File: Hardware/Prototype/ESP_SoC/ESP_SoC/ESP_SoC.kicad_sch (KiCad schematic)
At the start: 35 parts, among them J1 USB_A, J2 Conn_01x01, J3 Conn_01x01, P1 USB_C_Plug, SW1 RESET, SW2 BOOT, U1 AP2112K-3.3, U2 ESP32-S3FN8, Y1 40MHz

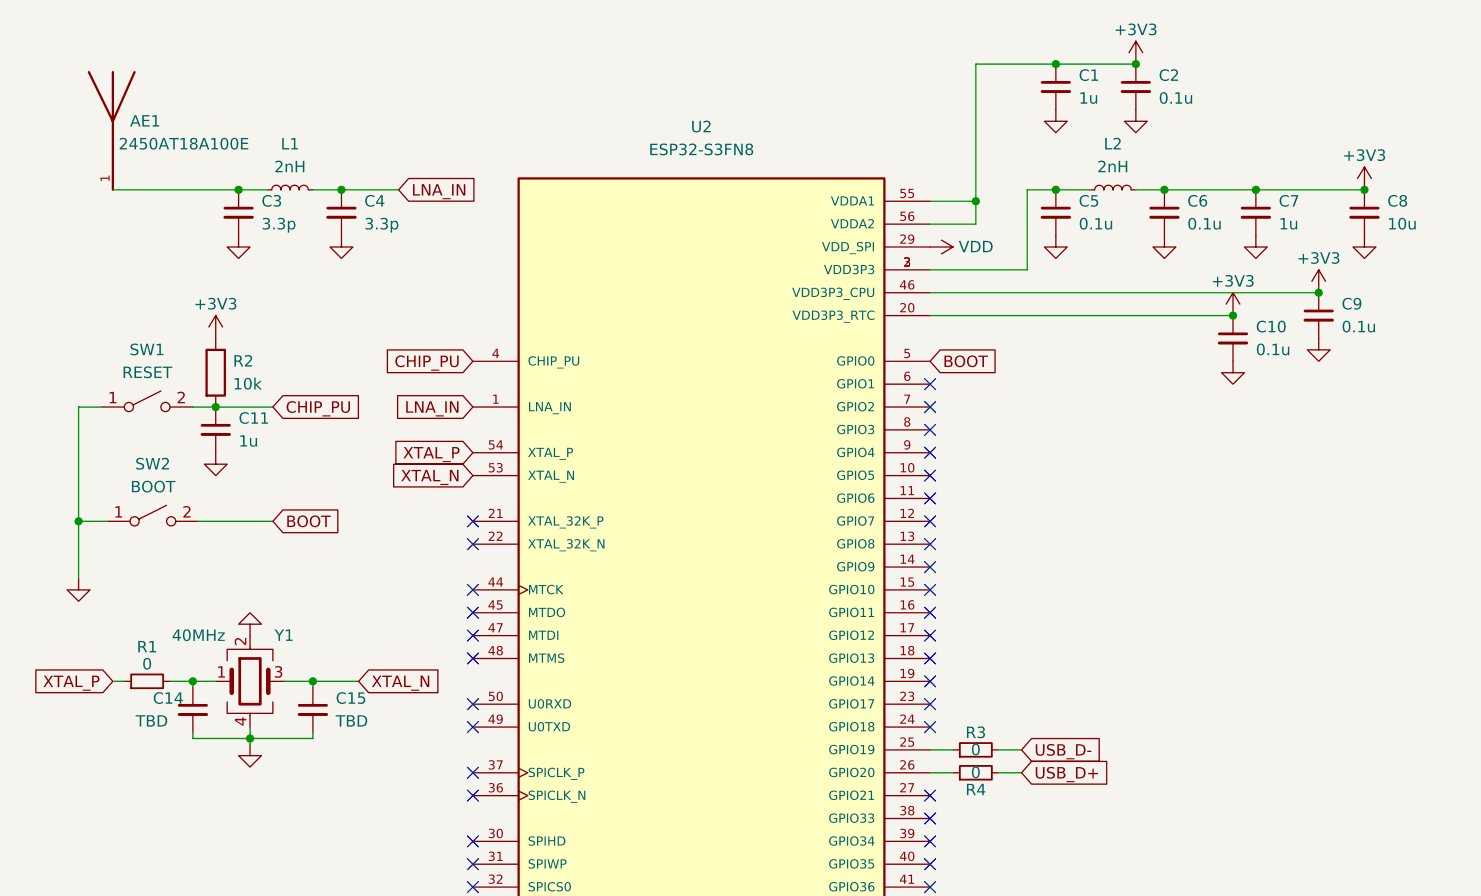
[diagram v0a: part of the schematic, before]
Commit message: Finished PCB prototypes and BOM
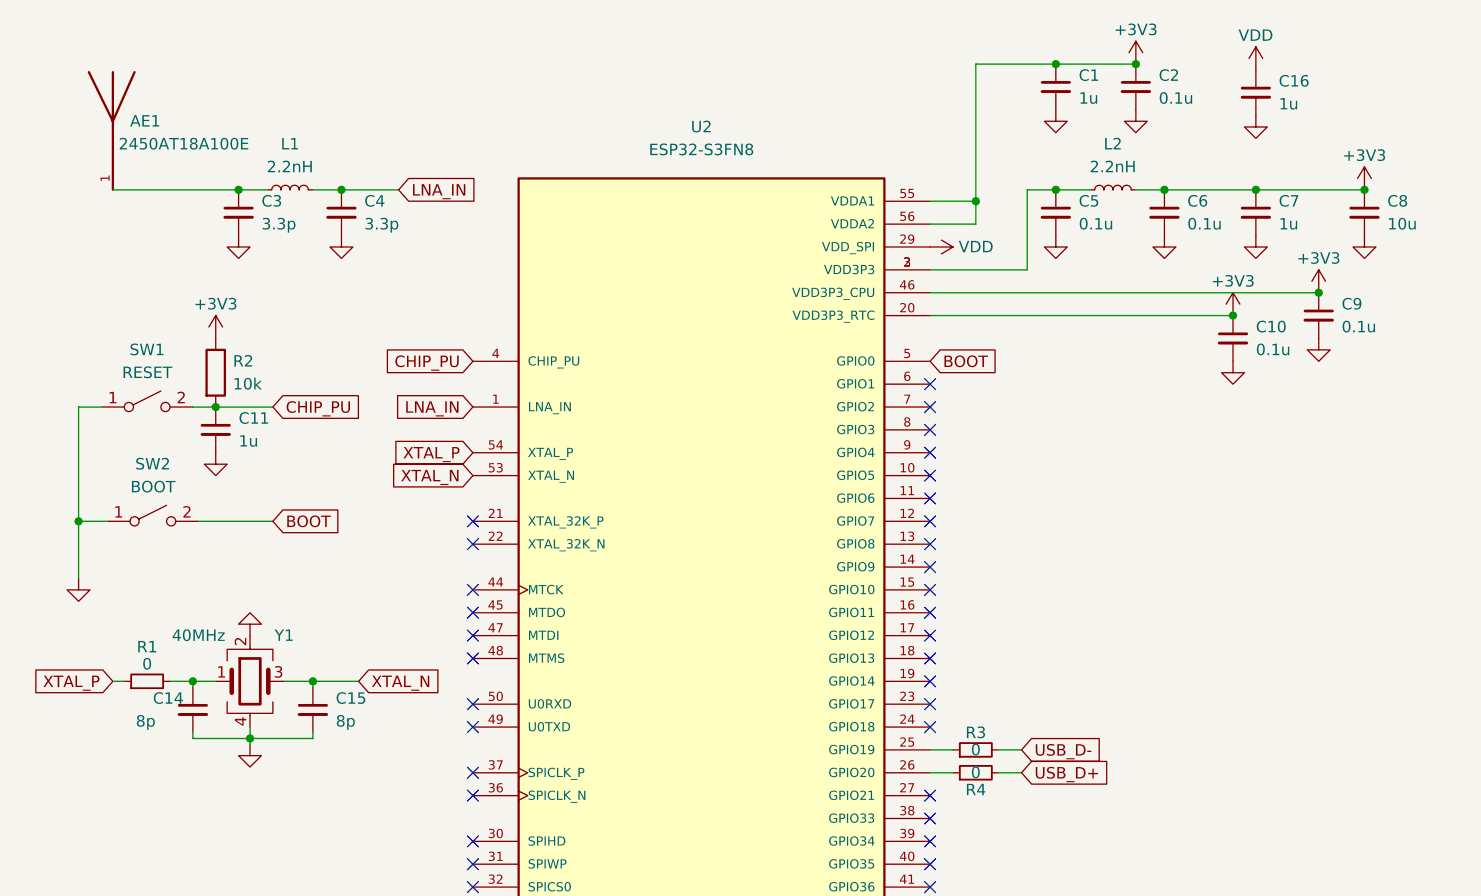
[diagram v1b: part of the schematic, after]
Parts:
- added C16: 1u, Capacitor_SMD:C_0402_1005Metric, symbol Device:C_Small
- AE1: LCSC Part (none) -> C89334; LCSC Part # (none) -> C89334
- C1, C11, C12, C13, C7: LCSC Part (none) -> C14445; LCSC Part # (none) -> C14445
- C10, C2, C5, C6, C9: LCSC Part (none) -> C1525; LCSC Part # (none) -> C1525
- C14, C15: value TBD -> 8p; LCSC Part (none) -> C281765; LCSC Part # (none) -> C281765
- C3, C4: LCSC Part (none) -> C415378; LCSC Part # (none) -> C415378
- C8: LCSC Part (none) -> C1691; LCSC Part # (none) -> C1691
- D1, D2: LCSC Part (none) -> C48192; LCSC Part # (none) -> C48192
- J1: LCSC Part (none) -> C136456; LCSC Part # (none) -> C136456
- L1, L2: value 2nH -> 2.2nH; LCSC Part (none) -> C91240; LCSC Part # (none) -> C91240
- P1: LCSC Part (none) -> C134082; LCSC Part # (none) -> C134082
- R1, R3, R4: LCSC Part (none) -> C21376; LCSC Part # (none) -> C21376
- R2: LCSC Part (none) -> C60490; LCSC Part # (none) -> C60490
- R5, R6: LCSC Part (none) -> C105872; LCSC Part # (none) -> C105872
- SW1: LCSC Part (none) -> C221897; LCSC Part # (none) -> C221897
- SW2: LCSC Part (none) -> C221896; LCSC Part # (none) -> C221896
- U1: LCSC Part (none) -> C51118; LCSC Part # (none) -> C51118
- Y1: LCSC Part (none) -> C187794; LCSC Part # (none) -> C187794
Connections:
- net GND: now also C16.2
- net VDD: now also C16.1

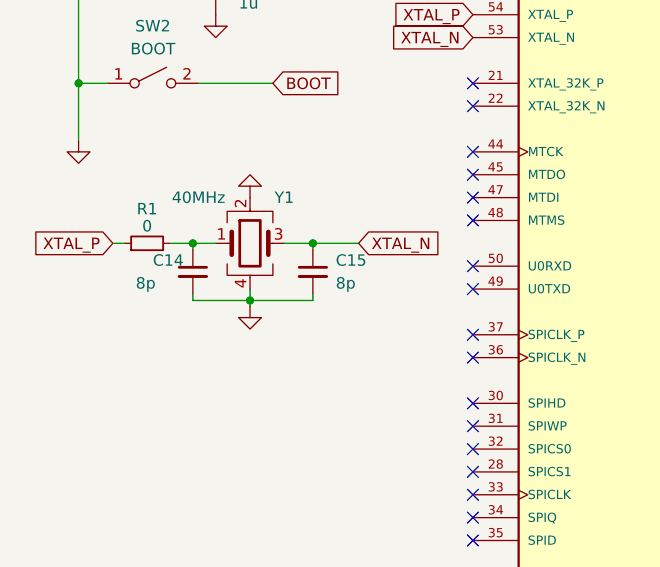
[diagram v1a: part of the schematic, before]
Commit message: Implemented ap + ws + usb hid backend
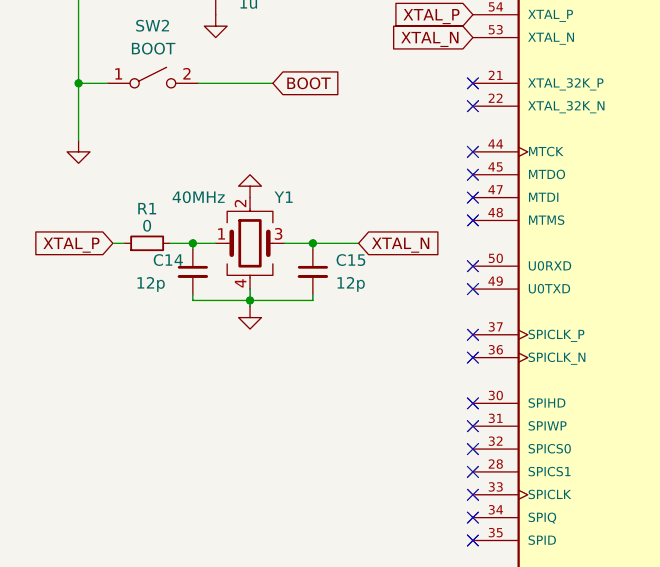
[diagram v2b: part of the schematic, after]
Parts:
- AE1: LCSC Part C89334 -> (none); LCSC Part # C89334 -> 609-2450AT18A100E
- C1, C11, C12, C13, C16, C7: LCSC Part C14445 -> (none); LCSC Part # C14445 -> (none)
- C10, C2, C5, C6, C9: LCSC Part C1525 -> (none); LCSC Part # C1525 -> (none)
- C14, C15: value 8p -> 12p; LCSC Part C281765 -> (none); LCSC Part # C281765 -> (none)
- C3, C4: LCSC Part C415378 -> (none); LCSC Part # C415378 -> (none)
- C8: LCSC Part C1691 -> (none); LCSC Part # C1691 -> (none)
- D1, D2: LCSC Part C48192 -> (none); LCSC Part # C48192 -> 863-NSR0320MW2T3G
- J1: LCSC Part C136456 -> (none); LCSC Part # C136456 -> 640-USB1061-GF-L-A
- L1, L2: LCSC Part C91240 -> (none); LCSC Part # C91240 -> 810-MLG1005S2N2BTD25
- P1: LCSC Part C134082 -> (none); LCSC Part # C134082 -> 538-105444-0001
- R1, R3, R4: LCSC Part C21376 -> (none); LCSC Part # C21376 -> (none)
- R2: LCSC Part C60490 -> (none); LCSC Part # C60490 -> (none)
- R5, R6: LCSC Part C105872 -> (none); LCSC Part # C105872 -> (none)
- SW1: LCSC Part C221897 -> (none); LCSC Part # C221897 -> 611-PTS810SJM250SMTR
- SW2: LCSC Part C221896 -> (none); LCSC Part # C221896 -> 611-PTS810SJM250SMTR
- U1: LCSC Part C51118 -> (none); LCSC Part # C51118 -> 621-AP2112K-3.3TRG1
- U2: LCSC Part # (none) -> 356-ESP32-S3FN8
- Y1: LCSC Part C187794 -> (none); LCSC Part # C187794 -> 520-400-10-37B2CKYTR
